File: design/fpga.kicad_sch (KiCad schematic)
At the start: 83 parts, among them J7 DEBUG_FPGA_GPIO, J8 DIGILENT_JTAG_HS2_01X06, SW1 RST, SW2 PROG, U13 XC7S15-FTGB196, U14 IS25LP064A-JKx

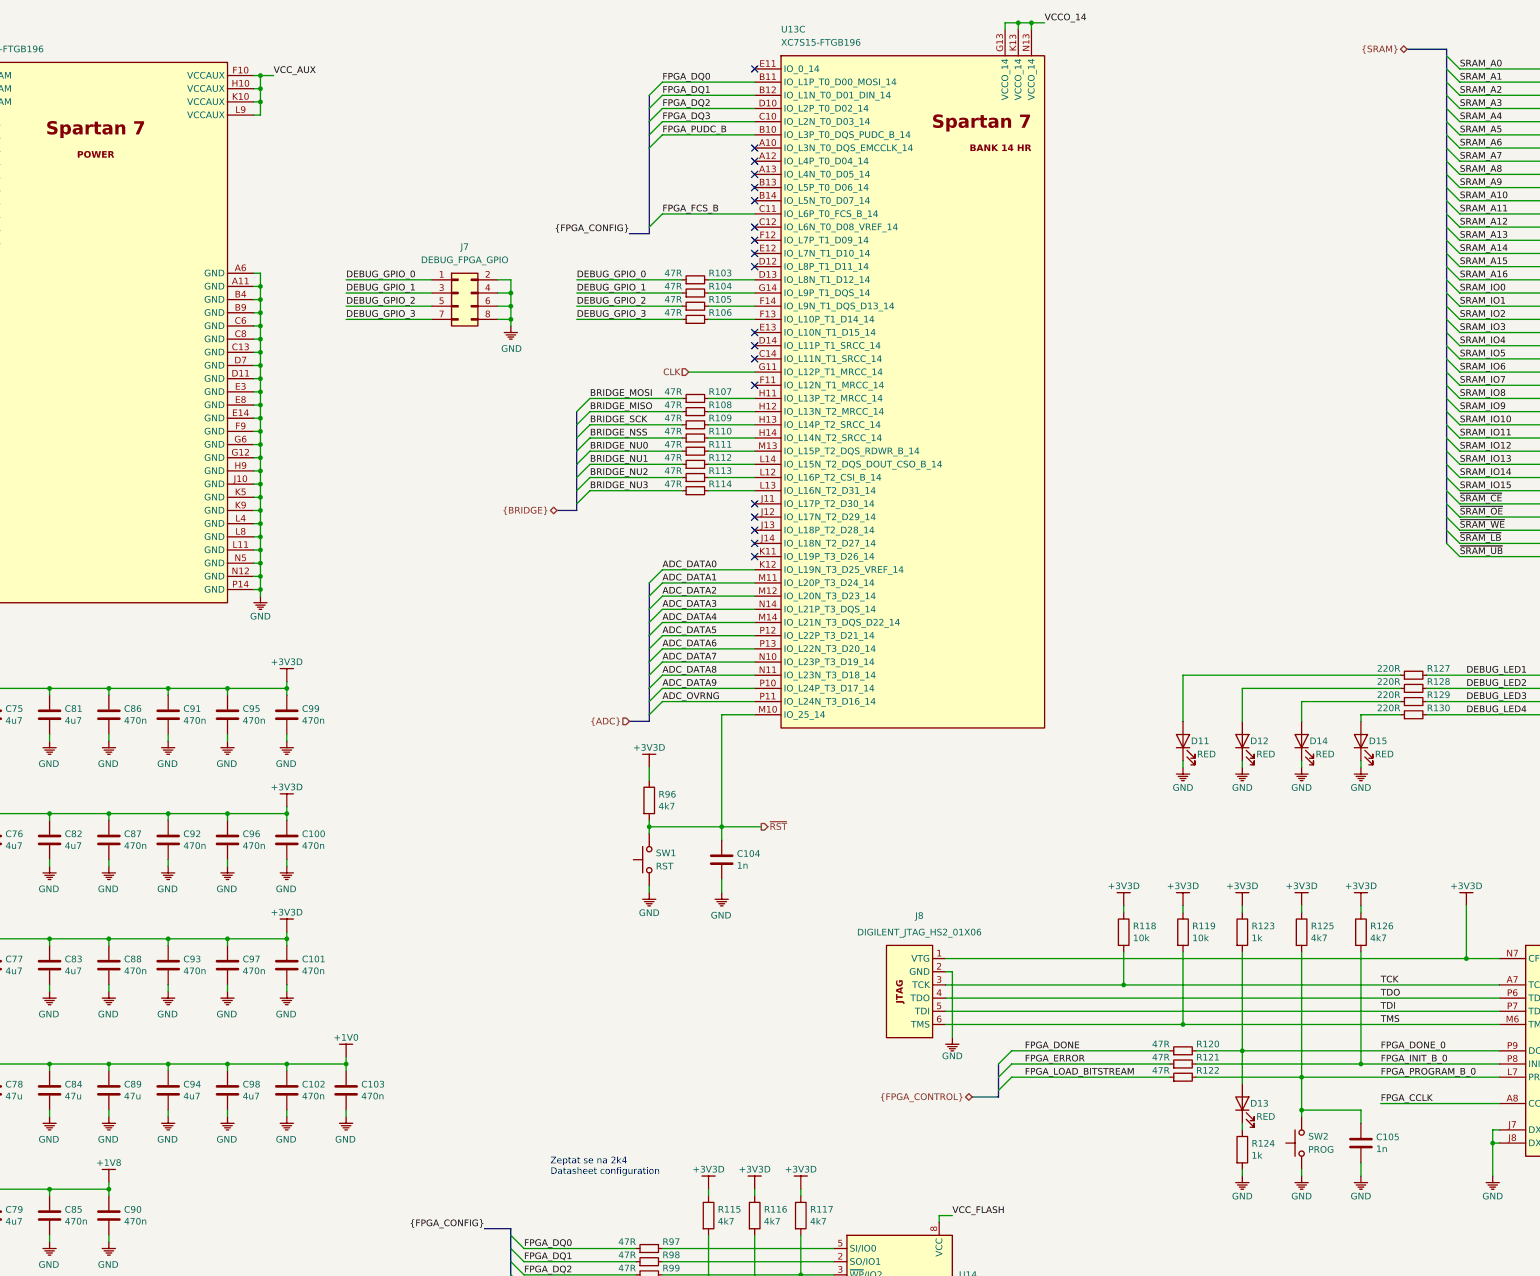
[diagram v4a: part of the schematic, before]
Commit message: Added FPGA placement
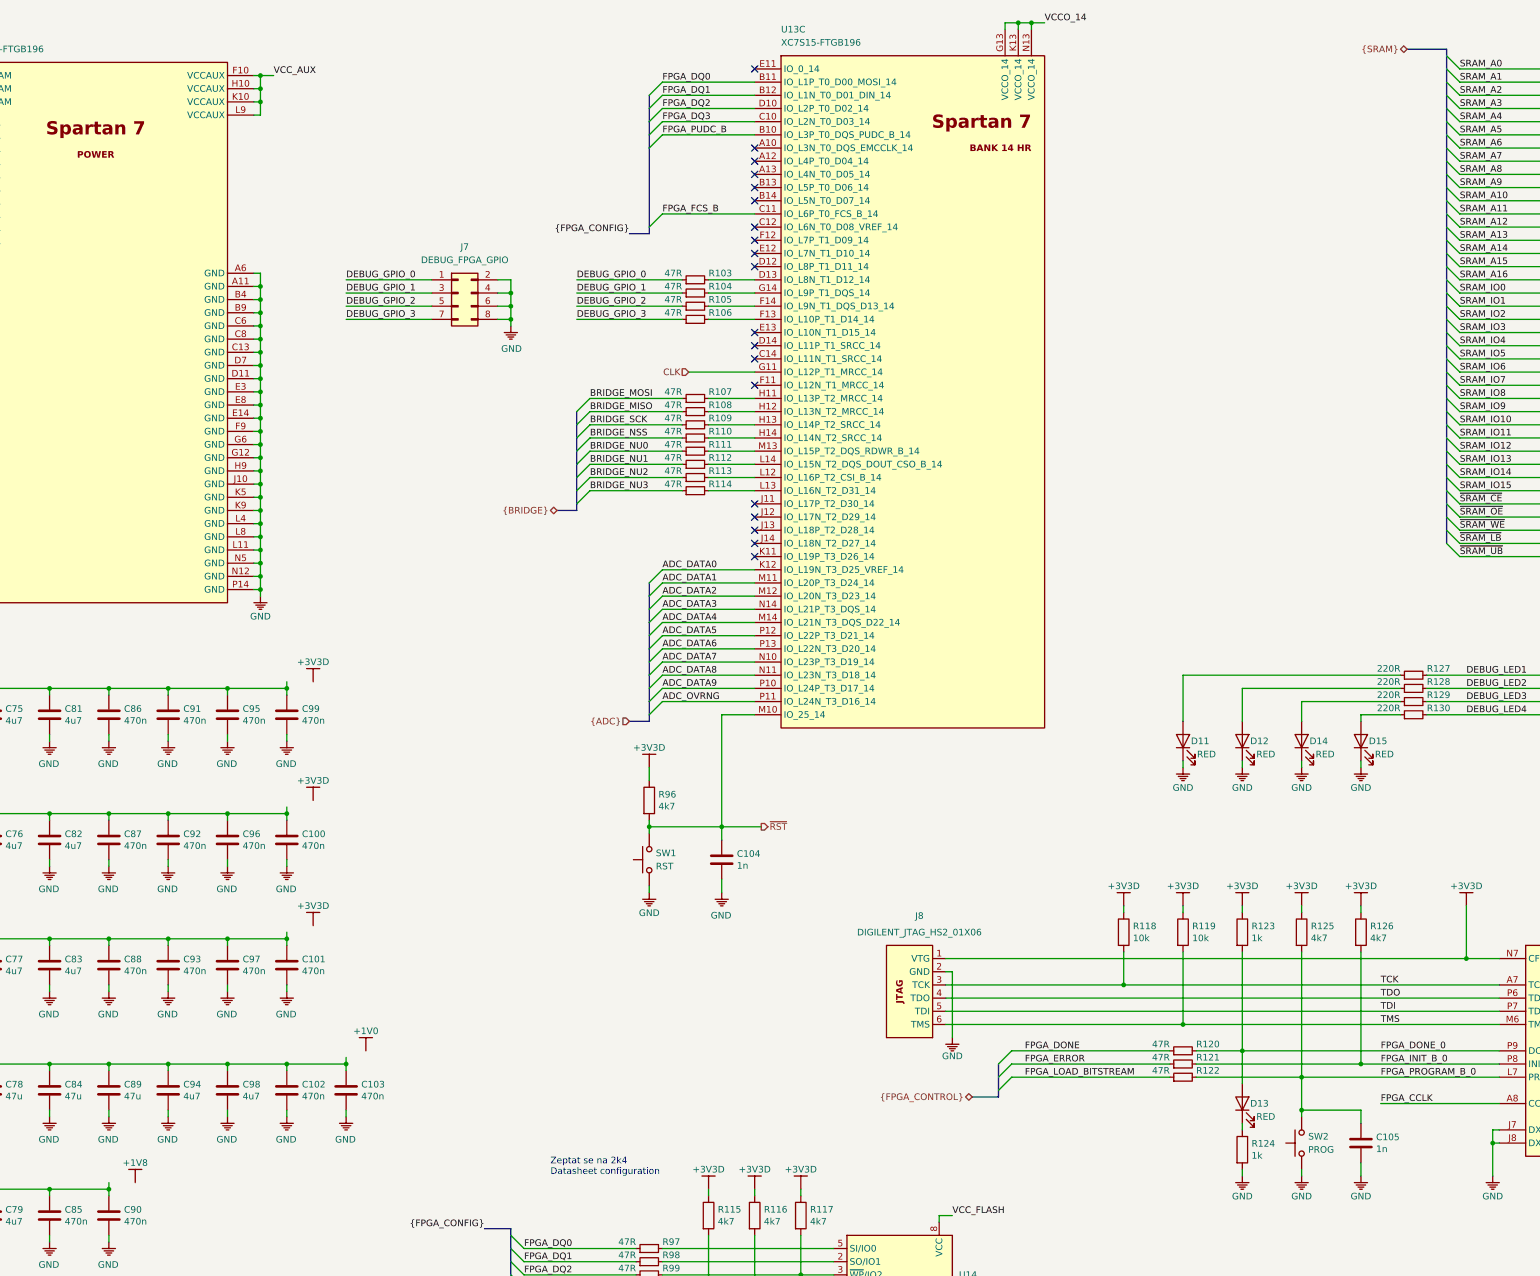
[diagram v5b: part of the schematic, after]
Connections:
- net +1V0: no longer C102.1, C103.1, C72.1, C78.1, C84.1, C89.1, C94.1, C98.1, U13.D6 (VCCINT), U13.D8 (VCCINT), U13.E5 (VCCBRAM), U13.E7 (VCCINT), U13.E9 (VCCINT), U13.F6 (VCCINT), U13.G5 (VCCBRAM), U13.G9 (VCCINT), U13.H6 (VCCINT), U13.J5 (VCCBRAM), U13.J9 (VCCINT), U13.K6 (VCCINT), U13.K8 (VCCINT)
- net +1V8: no longer C73.1, C79.1, C85.1, C90.1, U13.F10 (VCCAUX), U13.H10 (VCCAUX), U13.K10 (VCCAUX), U13.L9 (VCCAUX)
- net +3V3D: no longer C100.1, C101.1, C69.1, C70.1, C71.1, C75.1, C76.1, C77.1, C81.1, C82.1, C83.1, C86.1, C87.1, C88.1, C91.1, C92.1, C93.1, C95.1, C96.1, C97.1, C99.1, U13.G13 (VCCO_14), U13.G2 (VCCO_34), U13.K13 (VCCO_14), U13.K2 (VCCO_34), U13.N13 (VCCO_14), U13.N2 (VCCO_34), U13.N6 (VCCO_0), U13.N8 (VCCO_0)
- new net VCCO_0: C101.1, C71.1, C77.1, C83.1, C88.1, C93.1, C97.1, U13.N6 (VCCO_0), U13.N8 (VCCO_0)
- new net VCCO_14: C100.1, C70.1, C76.1, C82.1, C87.1, C92.1, C96.1, U13.G13 (VCCO_14), U13.K13 (VCCO_14), U13.N13 (VCCO_14)
- new net VCCO_34: C69.1, C75.1, C81.1, C86.1, C91.1, C95.1, C99.1, U13.G2 (VCCO_34), U13.K2 (VCCO_34), U13.N2 (VCCO_34)
- new net VCC_AUX: C73.1, C79.1, C85.1, C90.1, U13.F10 (VCCAUX), U13.H10 (VCCAUX), U13.K10 (VCCAUX), U13.L9 (VCCAUX)
- new net VCC_INT: C102.1, C103.1, C72.1, C78.1, C84.1, C89.1, C94.1, C98.1, U13.D6 (VCCINT), U13.D8 (VCCINT), U13.E5 (VCCBRAM), U13.E7 (VCCINT), U13.E9 (VCCINT), U13.F6 (VCCINT), U13.G5 (VCCBRAM), U13.G9 (VCCINT), U13.H6 (VCCINT), U13.J5 (VCCBRAM), U13.J9 (VCCINT), U13.K6 (VCCINT), U13.K8 (VCCINT)
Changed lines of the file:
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@@
   (bus (pts (xy 151.13 91.44) (xy 151.13 96.52)))
   (bus (pts (xy 151.13 96.52) (xy 151.13 101.6)))
-  (bus (pts (xy 151.13 101.6) (xy 151.13 106.68)))
-  (bus (pts (xy 151.13 106.68) (xy 151.13 110.49)))
+  (bus (pts (xy 151.13 101.6) (xy 151.13 104.14)))
+  (bus (pts (xy 151.13 104.14) (xy 151.13 109.22)))
+  (bus (pts (xy 151.13 109.22) (xy 151.13 110.49)))
   (bus (pts (xy 161.29 57.15) (xy 165.1 57.15)))
   (bus (pts (xy 161.29 151.13) (xy 165.1 151.13)))
@@
   (bus (pts (xy 165.1 35.56) (xy 165.1 40.64)))
   (bus (pts (xy 165.1 40.64) (xy 165.1 57.15)))
-  (bus (pts (xy 165.1 124.46) (xy 165.1 129.54)))
-  (bus (pts (xy 165.1 129.54) (xy 165.1 134.62)))
-  (bus (pts (xy 165.1 134.62) (xy 165.1 139.7)))
-  (bus (pts (xy 165.1 139.7) (xy 165.1 144.78)))
-  (bus (pts (xy 165.1 144.78) (xy 165.1 149.86)))
-  (bus (pts (xy 165.1 149.86) (xy 165.1 151.13)))
+  (bus (pts (xy 165.1 124.46) (xy 165.1 127)))
+  (bus (pts (xy 165.1 127) (xy 165.1 132.08)))
+  (bus (pts (xy 165.1 132.08) (xy 165.1 137.16)))
+  (bus (pts (xy 165.1 137.16) (xy 165.1 142.24)))
+  (bus (pts (xy 165.1 142.24) (xy 165.1 147.32)))
+  (bus (pts (xy 165.1 147.32) (xy 165.1 151.13)))
   (bus (pts (xy 227.33 223.52) (xy 232.41 223.52)))
   (bus (pts (xy 232.41 217.17) (xy 232.41 222.25)))
@@
   (bus (pts (xy 318.77 21.59) (xy 311.15 21.59)))
   (bus (pts (xy 318.77 21.59) (xy 318.77 25.4)))
-  (bus (pts (xy 318.77 25.4) (xy 318.77 30.48)))
-  (bus (pts (xy 318.77 30.48) (xy 318.77 35.56)))
+  (bus (pts (xy 318.77 25.4) (xy 318.77 27.94)))
+  (bus (pts (xy 318.77 27.94) (xy 318.77 33.02)))
+  (bus (pts (xy 318.77 33.02) (xy 318.77 35.56)))
   (bus (pts (xy 318.77 35.56) (xy 318.77 40.64)))
   (bus (pts (xy 318.77 40.64) (xy 318.77 45.72)))
@@
   (bus (pts (xy 318.77 55.88) (xy 318.77 58.42)))
   (bus (pts (xy 318.77 58.42) (xy 318.77 63.5)))
-  (bus (pts (xy 318.77 63.5) (xy 318.77 66.04)))
-  (bus (pts (xy 318.77 66.04) (xy 318.77 71.12)))
-  (bus (pts (xy 318.77 71.12) (xy 318.77 76.2)))
-  (bus (pts (xy 318.77 76.2) (xy 318.77 81.28)))
-  (bus (pts (xy 318.77 81.28) (xy 318.77 86.36)))
-  (bus (pts (xy 318.77 86.36) (xy 318.77 91.44)))
-  (bus (pts (xy 318.77 91.44) (xy 318.77 96.52)))
-  (bus (pts (xy 318.77 96.52) (xy 318.77 101.6)))
-  (bus (pts (xy 318.77 101.6) (xy 318.77 104.14)))
-  (bus (pts (xy 318.77 104.14) (xy 318.77 109.22)))
-  (bus (pts (xy 318.77 109.22) (xy 318.77 111.76)))
+  (bus (pts (xy 318.77 63.5) (xy 318.77 68.58)))
+  (bus (pts (xy 318.77 68.58) (xy 318.77 73.66)))
+  (bus (pts (xy 318.77 73.66) (xy 318.77 78.74)))
+  (bus (pts (xy 318.77 78.74) (xy 318.77 83.82)))
+  (bus (pts (xy 318.77 83.82) (xy 318.77 88.9)))
+  (bus (pts (xy 318.77 88.9) (xy 318.77 93.98)))
+  (bus (pts (xy 318.77 93.98) (xy 318.77 99.06)))
+  (bus (pts (xy 318.77 99.06) (xy 318.77 101.6)))
+  (bus (pts (xy 318.77 101.6) (xy 318.77 106.68)))
+  (bus (pts (xy 318.77 106.68) (xy 318.77 111.76)))
   (bus (pts (xy 318.77 111.76) (xy 318.77 116.84)))
   (text "Během konfigurovaí\nnastaví PULLUP pro IO" (at 129.54 278.13 0)
@@
     )
   )
-  (symbol (lib_id "KLIB_Power:+1V8") (at 60.96 240.03 0) (unit 1)
-    (property "Reference" "#PWR0164" (id 0) (at 60.96 247.65 0)
-      (effects (font (size 1.27 1.27)) hide)
-    )
-    (property "Value" "+1V8" (id 1) (at 60.96 236.22 0))
-    (property "Footprint" "" (id 2) (at 60.96 240.03 0)
-      (effects (font (size 1.27 1.27)) hide)
-    )
-    (property "Datasheet" "" (id 3) (at 60.96 240.03 0)
-      (effects (font (size 1.27 1.27)) hide)
-    )
-  )
   (symbol (lib_id "KLIB_Power:GND") (at 60.96 251.46 0) (mirror y) (unit 1)
     (property "Reference" "#PWR0165" (id 0) (at 60.96 256.54 0)
@@
     )
   )
+  (symbol (lib_id "KLIB_Power:+1V8") (at 66.04 240.03 0) (unit 1)
+    (property "Reference" "#PWR0164" (id 0) (at 66.04 247.65 0)
+      (effects (font (size 1.27 1.27)) hide)
+    )
+    (property "Value" "+1V8" (id 1) (at 66.04 236.22 0))
+    (property "Footprint" "" (id 2) (at 66.04 240.03 0)
+      (effects (font (size 1.27 1.27)) hide)
+    )
+    (property "Datasheet" "" (id 3) (at 66.04 240.03 0)
+      (effects (font (size 1.27 1.27)) hide)
+    )
+  )
   (symbol (lib_id "KLIB_Power:GND") (at 72.39 154.94 0) (mirror y) (unit 1)
     (property "Reference" "#PWR0166" (id 0) (at 72.39 160.02 0)
@@
     )
   )
-  (symbol (lib_id "KLIB_Power:+3V3D") (at 95.25 143.51 0) (unit 1)
-    (property "Reference" "#PWR0175" (id 0) (at 95.25 151.13 0)
-      (effects (font (size 1.27 1.27)) hide)
-    )
-    (property "Value" "+3V3D" (id 1) (at 95.25 139.7 0))
-    (property "Footprint" "" (id 2) (at 95.25 143.51 0)
-      (effects (font (size 1.27 1.27)) hide)
-    )
-    (property "Datasheet" "" (id 3) (at 95.25 143.51 0)
-      (effects (font (size 1.27 1.27)) hide)
-    )
-  )
   (symbol (lib_id "KLIB_Power:GND") (at 95.25 154.94 0) (mirror y) (unit 1)
     (property "Reference" "#PWR0176" (id 0) (at 95.25 160.02 0)
@@
     )
   )
-  (symbol (lib_id "KLIB_Power:+3V3D") (at 95.25 167.64 0) (unit 1)
-    (property "Reference" "#PWR0177" (id 0) (at 95.25 175.26 0)
-      (effects (font (size 1.27 1.27)) hide)
-    )
-    (property "Value" "+3V3D" (id 1) (at 95.25 163.83 0))
-    (property "Footprint" "" (id 2) (at 95.25 167.64 0)
-      (effects (font (size 1.27 1.27)) hide)
-    )
-    (property "Datasheet" "" (id 3) (at 95.25 167.64 0)
-      (effects (font (size 1.27 1.27)) hide)
-    )
-  )
   (symbol (lib_id "KLIB_Power:GND") (at 95.25 179.07 0) (mirror y) (unit 1)
     (property "Reference" "#PWR0178" (id 0) (at 95.25 184.15 0)
@@
     )
   )
-  (symbol (lib_id "KLIB_Power:+3V3D") (at 95.25 191.77 0) (unit 1)
-    (property "Reference" "#PWR0179" (id 0) (at 95.25 199.39 0)
-      (effects (font (size 1.27 1.27)) hide)
-    )
-    (property "Value" "+3V3D" (id 1) (at 95.25 187.96 0))
-    (property "Footprint" "" (id 2) (at 95.25 191.77 0)
-      (effects (font (size 1.27 1.27)) hide)
-    )
-    (property "Datasheet" "" (id 3) (at 95.25 191.77 0)
-      (effects (font (size 1.27 1.27)) hide)
-    )
-  )
   (symbol (lib_id "KLIB_Power:GND") (at 95.25 203.2 0) (mirror y) (unit 1)
     (property "Reference" "#PWR0180" (id 0) (at 95.25 208.28 0)
@@
     )
   )
-  (symbol (lib_id "KLIB_Power:+1V0") (at 106.68 215.9 0) (unit 1)
-    (property "Reference" "#PWR0182" (id 0) (at 106.68 223.52 0)
-      (effects (font (size 1.27 1.27)) hide)
-    )
-    (property "Value" "+1V0" (id 1) (at 106.68 212.09 0))
-    (property "Footprint" "" (id 2) (at 106.68 215.9 0)
-      (effects (font (size 1.27 1.27)) hide)
-    )
-    (property "Datasheet" "" (id 3) (at 106.68 215.9 0)
+  (symbol (lib_id "KLIB_Power:+3V3D") (at 100.33 143.51 0) (unit 1)
+    (property "Reference" "#PWR0175" (id 0) (at 100.33 151.13 0)
+      (effects (font (size 1.27 1.27)) hide)
+    )
+    (property "Value" "+3V3D" (id 1) (at 100.33 139.7 0))
+    (property "Footprint" "" (id 2) (at 100.33 143.51 0)
+      (effects (font (size 1.27 1.27)) hide)
+    )
+    (property "Datasheet" "" (id 3) (at 100.33 143.51 0)
+      (effects (font (size 1.27 1.27)) hide)
+    )
+  )
+  (symbol (lib_id "KLIB_Power:+3V3D") (at 100.33 166.37 0) (unit 1)
+    (property "Reference" "#PWR0177" (id 0) (at 100.33 173.99 0)
+      (effects (font (size 1.27 1.27)) hide)
+    )
+    (property "Value" "+3V3D" (id 1) (at 100.33 162.56 0))
+    (property "Footprint" "" (id 2) (at 100.33 166.37 0)
+      (effects (font (size 1.27 1.27)) hide)
+    )
+    (property "Datasheet" "" (id 3) (at 100.33 166.37 0)
+      (effects (font (size 1.27 1.27)) hide)
+    )
+  )
+  (symbol (lib_id "KLIB_Power:+3V3D") (at 100.33 190.5 0) (unit 1)
+    (property "Reference" "#PWR0179" (id 0) (at 100.33 198.12 0)
+      (effects (font (size 1.27 1.27)) hide)
+    )
+    (property "Value" "+3V3D" (id 1) (at 100.33 186.69 0))
+    (property "Footprint" "" (id 2) (at 100.33 190.5 0)
+      (effects (font (size 1.27 1.27)) hide)
+    )
+    (property "Datasheet" "" (id 3) (at 100.33 190.5 0)
       (effects (font (size 1.27 1.27)) hide)
     )
@@
       (effects (font (size 1.27 1.27)) hide)
     )
+  )
+  (symbol (lib_id "KLIB_Power:+1V0") (at 110.49 214.63 0) (unit 1)
+    (property "Reference" "#PWR0182" (id 0) (at 110.49 222.25 0)
+      (effects (font (size 1.27 1.27)) hide)
+    )
+    (property "Value" "+1V0" (id 1) (at 110.49 210.82 0))
+    (property "Footprint" "" (id 2) (at 110.49 214.63 0)
+      (effects (font (size 1.27 1.27)) hide)
+    )
+    (property "Datasheet" "" (id 3) (at 110.49 214.63 0)
+      (effects (font (size 1.27 1.27)) hide)
+    )
